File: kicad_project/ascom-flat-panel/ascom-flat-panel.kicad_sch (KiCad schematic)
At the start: 12 parts, among them J1 Servo, J2 JST-XH LED, Q1 IRLZ34N, Q2 IRLZ34N, U1 XIAO-SAMD21-DIP

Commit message: [kicad] - Modification empreinte du Condensateur par cohérence avec les composants reçus (diam 6.3 au lieu de 5)
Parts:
- C1: footprint Capacitor_THT:CP_Radial_D5.0mm_P2.50mm -> Capacitor_THT:C_Radial_D6.3mm_H11.0mm_P2.50mm
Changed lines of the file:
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@@
 			)
 		)
-		(property "Footprint" "Capacitor_THT:CP_Radial_D5.0mm_P2.50mm"
+		(property "Footprint" "Capacitor_THT:C_Radial_D6.3mm_H11.0mm_P2.50mm"
 			(at 155.9052 53.34 0)
 			(effects

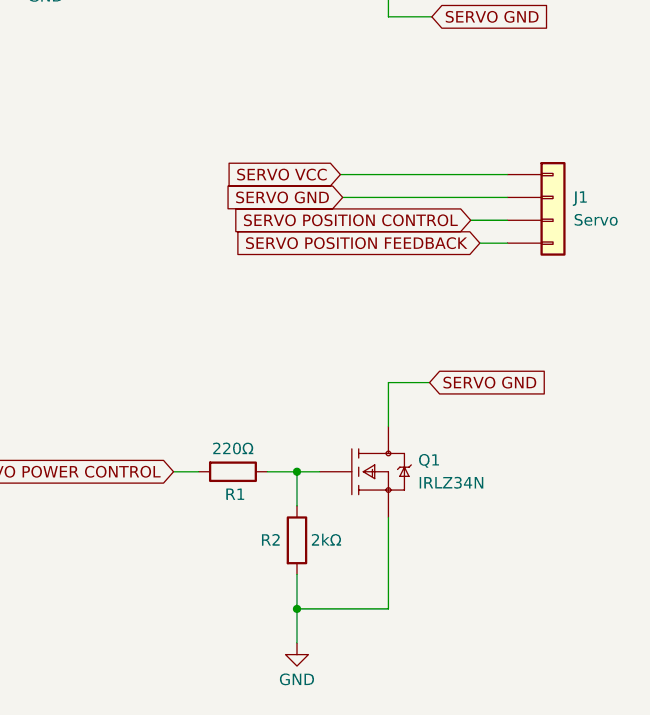
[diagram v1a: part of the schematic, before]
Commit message: [kicad] - Modif suite aux tests servo : valeur R2 + routage connecteur
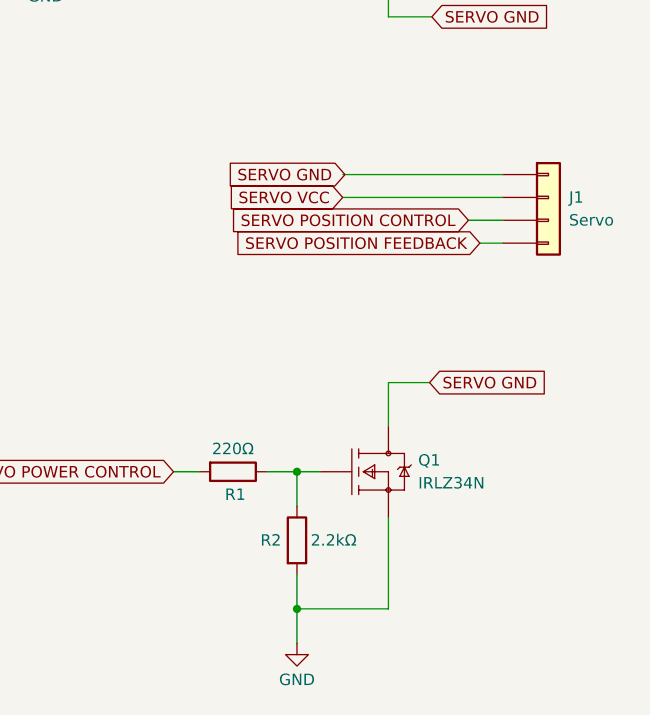
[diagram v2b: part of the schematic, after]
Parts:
- R2: value 2kΩ -> 2.2kΩ
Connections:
- net SERVO GND: now also J1.1 (Pin_1); no longer J1.2 (Pin_2)
- net SERVO VCC: now also J1.2 (Pin_2); no longer J1.1 (Pin_1)
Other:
- moved on the sheet: J1
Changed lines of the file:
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@@
-	(wire
-		(pts
-			(xy 187.96 81.28) (xy 206.248 81.28)
-		)
-		(stroke
-			(width 0)
-			(type default)
-		)
-	)
 	(wire
 		(pts
@@
 	(wire
 		(pts
-			(xy 203.2 86.36) (xy 206.248 86.36)
+			(xy 203.2 86.36) (xy 205.74 86.36)
 		)
 		(stroke
@@
 	(wire
 		(pts
+			(xy 187.96 81.28) (xy 205.74 81.28)
+		)
+		(stroke
+			(width 0)
+			(type default)
+		)
+	)
+	(wire
+		(pts
 			(xy 54.61 67.31) (xy 63.5 67.31)
 		)
@@
 	(wire
 		(pts
+			(xy 187.96 78.74) (xy 205.74 78.74)
+		)
+		(stroke
+			(width 0)
+			(type default)
+		)
+	)
+	(wire
+		(pts
 			(xy 88.9 127) (xy 88.9 116.84)
 		)
@@
 	(wire
 		(pts
-			(xy 187.706 78.74) (xy 206.248 78.74)
-		)
-		(stroke
-			(width 0)
-			(type default)
-		)
-	)
-	(wire
-		(pts
 			(xy 193.04 127) (xy 182.88 127)
 		)
@@
 	(wire
 		(pts
-			(xy 202.184 83.82) (xy 206.248 83.82)
+			(xy 201.93 83.82) (xy 205.74 83.82)
 		)
 		(stroke
@@
 	(global_label "SERVO GND"
 		(shape input)
+		(at 188.214 78.74 180)
+		(fields_autoplaced yes)
+		(effects
+			(font
+				(size 1.27 1.27)
+			)
+			(justify right)
+		)
+		(property "Intersheetrefs" "${INTERSHEET_REFS}"
+			(at 174.3431 78.74 0)
+			(effects
+				(font
+					(size 1.27 1.27)
+				)
+				(justify right)
+				(hide yes)
+			)
+		)
+	)
+	(global_label "SERVO POWER CONTROL"
+		(shape input)
+		(at 54.61 59.69 180)
+		(fields_autoplaced yes)
+		(effects
+			(font
+				(size 1.27 1.27)
+			)
+			(justify right)
+		)
+		(property "Intersheetrefs" "${INTERSHEET_REFS}"
+			(at 28.6439 59.69 0)
+			(effects
+				(font
+					(size 1.27 1.27)
+				)
+				(justify right)
+				(hide yes)
+			)
+		)
+	)
+	(global_label "SERVO POSITION CONTROL"
+		(shape input)
+		(at 54.61 63.5 180)
+		(fields_autoplaced yes)
+		(effects
+			(font
+				(size 1.27 1.27)
+			)
+			(justify right)
+		)
+		(property "Intersheetrefs" "${INTERSHEET_REFS}"
+			(at 26.4666 63.5 0)
+			(effects
+				(font
+					(size 1.27 1.27)
+				)
+				(justify right)
+				(hide yes)
+			)
+		)
+	)
+	(global_label "SERVO VCC"
+		(shape input)
 		(at 187.96 81.28 180)
 		(fields_autoplaced yes)
@@
 		)
 		(property "Intersheetrefs" "${INTERSHEET_REFS}"
-			(at 174.0891 81.28 0)
+			(at 174.331 81.28 0)
 			(effects
 				(font
@@
 		)
 	)
-	(global_label "SERVO POWER CONTROL"
-		(shape input)
-		(at 54.61 59.69 180)
+	(global_label "SERVO POSITION FEEDBACK"
+		(shape input)
+		(at 203.2 86.36 180)
 		(fields_autoplaced yes)
 		(effects
@@
 		)
 		(property "Intersheetrefs" "${INTERSHEET_REFS}"
-			(at 28.6439 59.69 0)
+			(at 174.0286 86.36 0)
 			(effects
 				(font
@@
 	(global_label "SERVO POSITION CONTROL"
 		(shape input)
-		(at 54.61 63.5 180)
+		(at 201.93 83.82 180)
 		(fields_autoplaced yes)
 		(effects
@@
 		)
 		(property "Intersheetrefs" "${INTERSHEET_REFS}"
-			(at 26.4666 63.5 0)
-			(effects
-				(font
-					(size 1.27 1.27)
-				)
-				(justify right)
-				(hide yes)
-			)
-		)
-	)
-	(global_label "SERVO VCC"
-		(shape input)
-		(at 187.706 78.74 180)
-		(fields_autoplaced yes)
-		(effects
-			(font
-				(size 1.27 1.27)
-			)
-			(justify right)
-		)
-		(property "Intersheetrefs" "${INTERSHEET_REFS}"
-			(at 174.077 78.74 0)
-			(effects
-				(font
-					(size 1.27 1.27)
-				)
-				(justify right)
-				(hide yes)
-			)
-		)
-	)
-	(global_label "SERVO POSITION FEEDBACK"
-		(shape input)
-		(at 203.2 86.36 180)
-		(fields_autoplaced yes)
-		(effects
-			(font
-				(size 1.27 1.27)
-			)
-			(justify right)
-		)
-		(property "Intersheetrefs" "${INTERSHEET_REFS}"
-			(at 174.0286 86.36 0)
-			(effects
-				(font
-					(size 1.27 1.27)
-				)
-				(justify right)
-				(hide yes)
-			)
-		)
-	)
-	(global_label "SERVO POSITION CONTROL"
-		(shape input)
-		(at 202.184 83.82 180)
-		(fields_autoplaced yes)
-		(effects
-			(font
-				(size 1.27 1.27)
-			)
-			(justify right)
-		)
-		(property "Intersheetrefs" "${INTERSHEET_REFS}"
-			(at 174.0406 83.82 0)
+			(at 173.7866 83.82 0)
 			(effects
 				(font
@@
 			)
 		)
-		(property "Value" "2kΩ"
+		(property "Value" "2.2kΩ"
 			(at 184.404 119.38 0)
 			(effects
@@
 	(symbol
 		(lib_id "Connector_Generic:Conn_01x04")
-		(at 211.328 81.28 0)
+		(at 210.82 81.28 0)
 		(unit 1)
 		(exclude_from_sim no)
@@
 		(fields_autoplaced yes)
 		(property "Reference" "J1"
-			(at 213.614 81.28 0)
+			(at 213.106 81.28 0)
 			(effects
 				(font
@@
 		)
 		(property "Value" "Servo"
-			(at 213.614 83.82 0)
+			(at 213.106 83.82 0)
 			(effects
 				(font
@@
 		)
 		(property "Footprint" "Connector_PinHeader_2.54mm:PinHeader_1x04_P2.54mm_Vertical"
-			(at 211.328 81.28 0)
+			(at 210.82 81.28 0)
 			(effects
 				(font
@@
 		)
 		(property "Datasheet" "~"
-			(at 211.328 81.28 0)
+			(at 210.82 81.28 0)
 			(effects
 				(font
@@
 		)
 		(property "Description" ""
-			(at 211.328 81.28 0)
-			(effects
-				(font
+			(at 210.82 81.28 0)
+			(effects
+				(font
